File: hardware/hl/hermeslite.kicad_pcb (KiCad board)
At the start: 4 copper layers, 150 x 100 mm, 291 parts, among them CN1 USBBlaster2, CN2 PS, CN3 MagJack, CN4 IO8, CN5 IO8, J1 JNC, J10 JNC, J11 JNC, J12 JNO, J13 JNO, J14 JNC, J16 JNO, J17 JNO, J18 JNC, J2 JNC, J22 JNC, J3 JNO, J4 JNO, J7 JNO, J8 JNO, J9 JNC, Q1 DMP3099L, T2 8:1 Z, U1 EEPROM, U16 ST1S10, U17 TPS730, U2 FPGA, U3 ST1S10, U4 KSZ9031RN, U5 MCP4716, U6 5P49V5923, U7 AD9866BCPZ, X1 25MHz, X2 38.4MHz, X3 38.4MHz

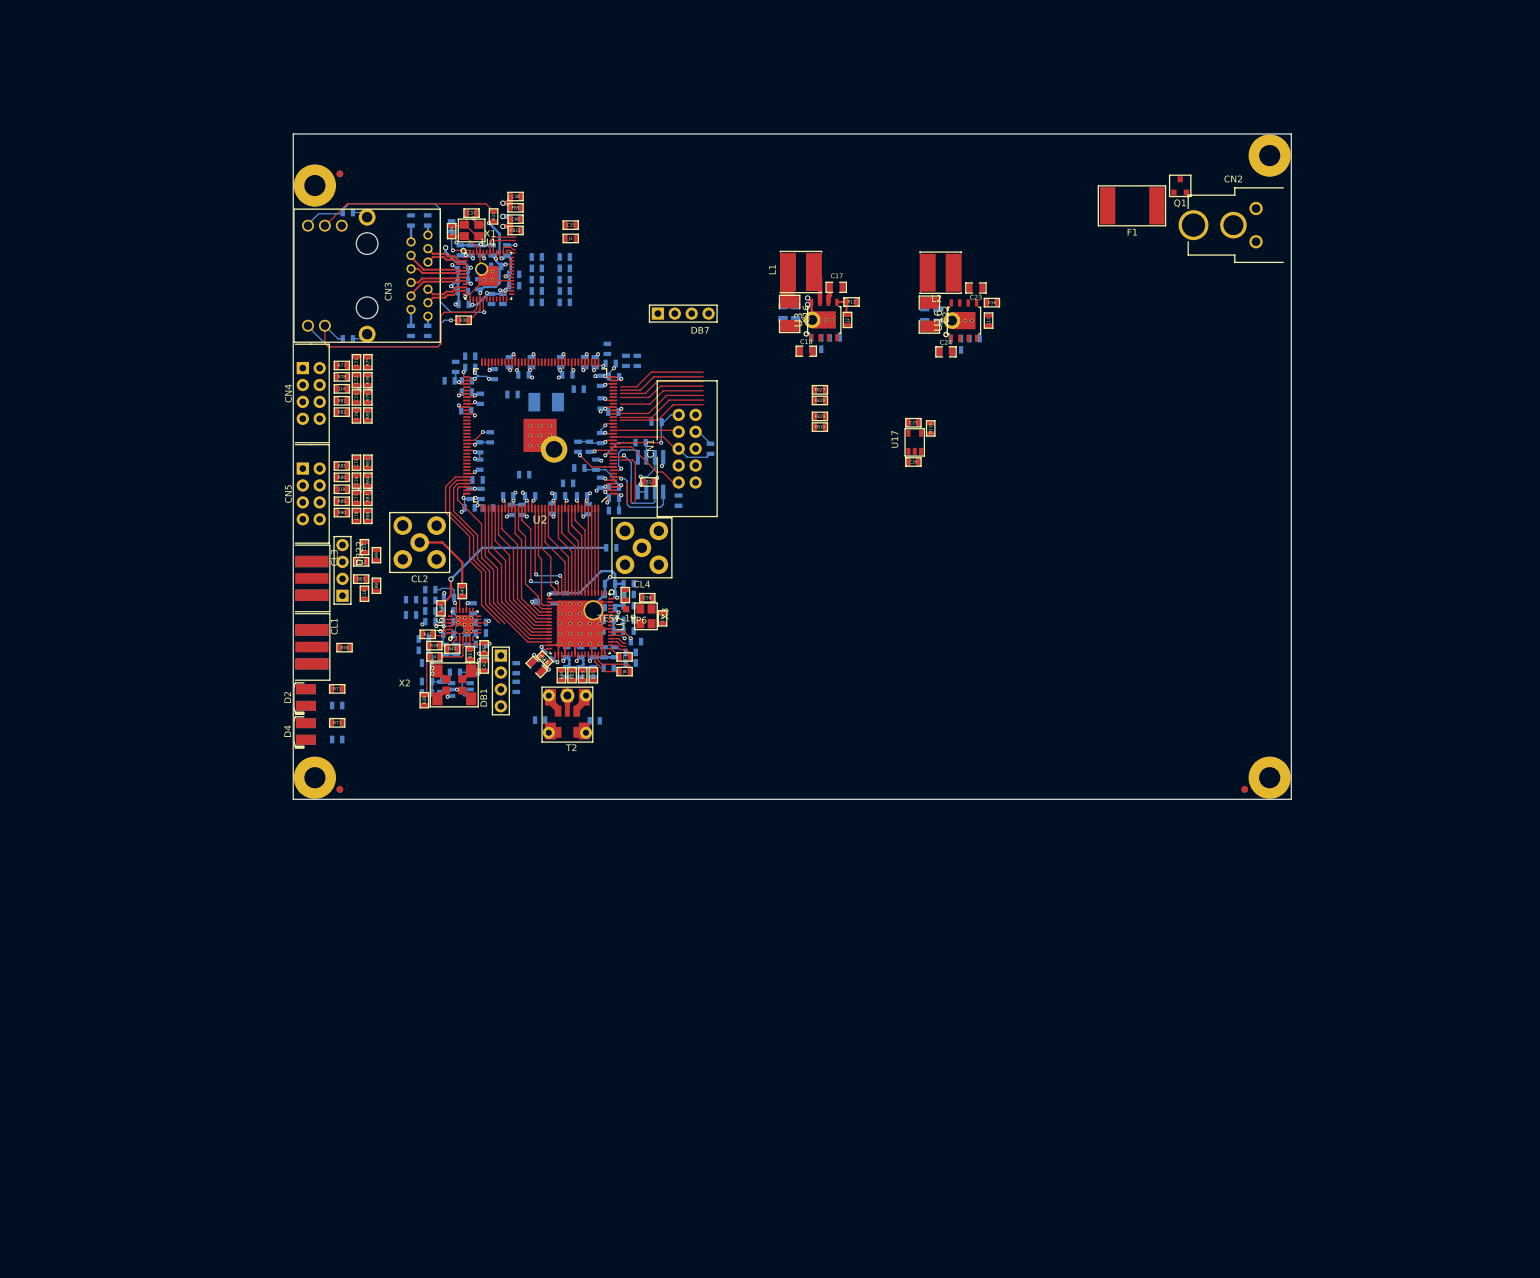
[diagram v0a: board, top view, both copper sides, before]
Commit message: Updates to layout
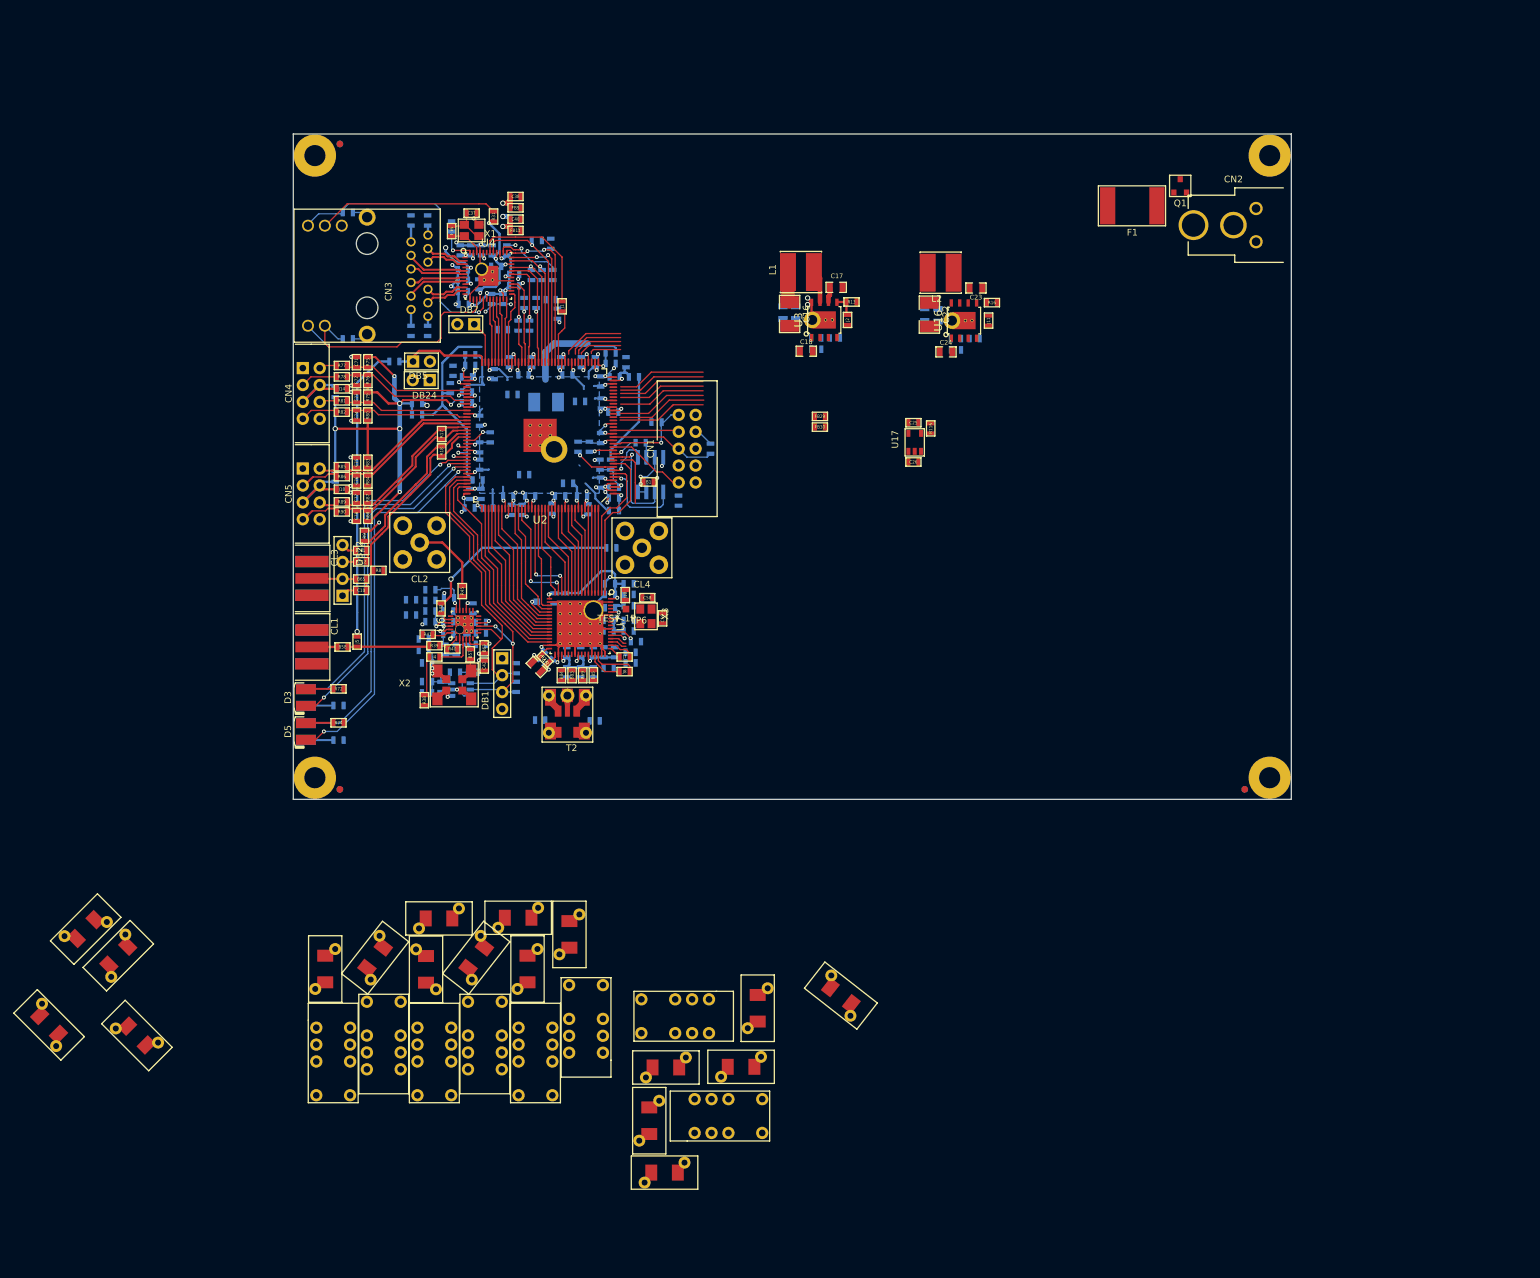
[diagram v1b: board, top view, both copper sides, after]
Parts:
- added DB24: RFD2b, HERMESLITE:2x1, F.Cu at (90.5, 77.0)
- added DB5: RFD2a, HERMESLITE:2x1, F.Cu at (88.0, 74.2)
- added J23: JNO, HERMESLITE:SMD-0603, B.Cu at (85.2, 74.2)
- added J5: JNO, HERMESLITE:SMD-0603, F.Cu at (79.6, 116.3)
- added R17: DNI, HERMESLITE:SMD-0603, F.Cu at (92.3, 85.1)
- added R18: DNI, HERMESLITE:SMD-0603, F.Cu at (92.3, 87.7)
- added REF**: inductor, HERMESLITE:inductor, F.Cu at (139.8, 171.4)
- added REF**: inductor, HERMESLITE:inductor, F.Cu at (105.2, 165.5)
- added REF**: DPDT, HERMESLITE:DPDT, F.Cu at (106.4, 179.4)
- added REF**: inductor, HERMESLITE:inductorrev, F.Cu at (90.0, 165.6)
- added REF**: DPDT, HERMESLITE:DPDT, F.Cu at (98.8, 175.5)
- added REF**: DPDT, HERMESLITE:DPDT, F.Cu at (91.2, 179.4)
- added REF**: inductor, HERMESLITE:inductorrev, F.Cu at (97.5, 163.8)
- added REF**: inductor, HERMESLITE:inductor, F.Cu at (152.3, 169.5)
- added REF**: inductor, HERMESLITE:inductorrev, F.Cu at (91.9, 157.9)
- added REF**: inductor, HERMESLITE:inductorrev, F.Cu at (126.0, 180.3)
- added REF**: inductor, HERMESLITE:inductor, F.Cu at (74.8, 165.5)
- added REF**: inductor, HERMESLITE:inductorrev, F.Cu at (137.3, 180.2)
- added REF**: inductor, HERMESLITE:inductor, F.Cu at (33.3, 173.9)
- added REF**: inductor, HERMESLITE:inductorrev, F.Cu at (46.5, 175.5)
- added REF**: inductor, HERMESLITE:inductorrev, F.Cu at (43.7, 163.5)
- added REF**: DPDT, HERMESLITE:DPDT, F.Cu at (83.6, 175.5)
- added REF**: inductor, HERMESLITE:inductor, F.Cu at (38.8, 159.5)
- added REF**: DPDT, HERMESLITE:DPDT, F.Cu at (76.0, 179.4)
- added REF**: inductor, HERMESLITE:inductorrev, F.Cu at (82.3, 163.8)
- added REF**: DPDT, HERMESLITE:DPDT, F.Cu at (127.4, 172.6)
- added REF**: inductor, HERMESLITE:inductorrev, F.Cu at (125.8, 196.1)
- added REF**: inductor, HERMESLITE:inductor, F.Cu at (123.5, 188.3)
- added REF**: inductor, HERMESLITE:inductor, F.Cu at (111.5, 160.3)
- added REF**: inductor, HERMESLITE:inductorrev, F.Cu at (103.8, 157.8)
- added REF**: DPDT, HERMESLITE:DPDT, F.Cu at (135.4, 187.6)
- added REF**: DPDT, HERMESLITE:DPDT, F.Cu at (114.0, 173.0)
- C35, D2, D4, FB27, FB28, R30, R71, R73: moved to B.Cu
- D3, D5, R72, R74: moved to F.Cu
- DB22: value RFD4d -> RFD4f
- DB7: value RFD4d -> RFD2b; footprint HERMESLITE:4x1 -> HERMESLITE:2x1
- moved FB28 60.6 mm to (88.6, 82.2), turned to 180 degrees
- moved FB27 60.6 mm to (88.6, 80.5), turned to 180 degrees
- moved DB7 27.6 mm to (97.2, 68.6), turned to 180 degrees
- moved C35 13.4 mm to (109.7, 67.0), turned to 270 degrees
- moved J1 10.3 mm to (110.4, 65.9), turned to 270 degrees
- moved R72 7.60 mm to (76.8, 123.4)
- moved R29 6.74 mm to (108.7, 64.9), turned to 180 degrees
- moved R22 6.10 mm to (104.7, 65.4), turned to 270 degrees
- moved R30 6.06 mm to (101.5, 69.4)
- moved R23 5.32 mm to (105.5, 68.8), turned to 90 degrees
- moved D3 5.10 mm to (70.9, 124.7), turned to 270 degrees
- moved D5 5.10 mm to (70.9, 129.8), turned to 270 degrees
- moved J17 4.79 mm to (76.3, 91.5), turned to 270 degrees
- moved FB6 4.73 mm to (117.7, 89.7), turned to 270 degrees
- moved R24 4.66 mm to (106.5, 65.4), turned to 270 degrees
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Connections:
- DB7 pad 1: Veth -> Net-(DB7-Pad1)
- DB7 pad 2: Net-(DB7-Pad2) -> GND
- R74 pad 1: Vlvds -> +3V3
- U2 pad 101: (no net) -> Net-(D5-Pad1)
- U2 pad 71: Net-(DB7-Pad2) -> Net-(DB7-Pad1)
- U2 pad 72: Net-(DB7-Pad3) -> Net-(DB5-Pad1)
- U2 pad 76: Net-(C71-Pad1) -> Net-(DB24-Pad1)
- U2 pad 77: Net-(C72-Pad1) -> Net-(C71-Pad1)
- U2 pad 80: Net-(C73-Pad1) -> Net-(C72-Pad1)
- U2 pad 83: Net-(C74-Pad1) -> Net-(C73-Pad1)
- U2 pad 85: Net-(D5-Pad1) -> Net-(C74-Pad1)
- U2 pad 90: Net-(B65-Pad2) -> Net-(B112-Pad2)
- U2 pad 91: Net-(B112-Pad2) -> Net-(B65-Pad2)
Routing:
- net Vlvds: track 2.21 -> 78.3 mm, vias 1 -> 7
- net Net-(D5-Pad1): track 0.00 -> 56.6 mm, vias 0 -> 2
- net Net-(D4-Pad1): track 0.00 -> 55.8 mm, vias 0 -> 1
- net Net-(D3-Pad1): track 0.00 -> 52.0 mm, vias 0 -> 2
- net Net-(D2-Pad1): track 0.00 -> 51.2 mm, vias 0 -> 1
- net +2V5: track 0.00 -> 48.3 mm, vias 0 -> 1
- net Net-(J23-Pad1): track 0.00 -> 44.3 mm, vias 0 -> 1
- net (no net): track 121.4 -> 162.9 mm
- net +1V2: track 53.3 -> 92.6 mm
- net Net-(B65-Pad2): track 0.00 -> 31.6 mm
- net Net-(B112-Pad2): track 0.00 -> 30.1 mm
- net GND: track 193.7 -> 218.9 mm, vias 56 -> 72
- net Net-(C78-Pad1): track 0.00 -> 24.9 mm
- net SCL: track 27.0 -> 51.7 mm, vias 0 -> 2
- net Net-(C77-Pad1): track 0.00 -> 24.6 mm
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- added copper zone on B.Cu, net +1V2
- added copper zone on In1.Cu, net GND
- added copper zone on In2.Cu, net Veth

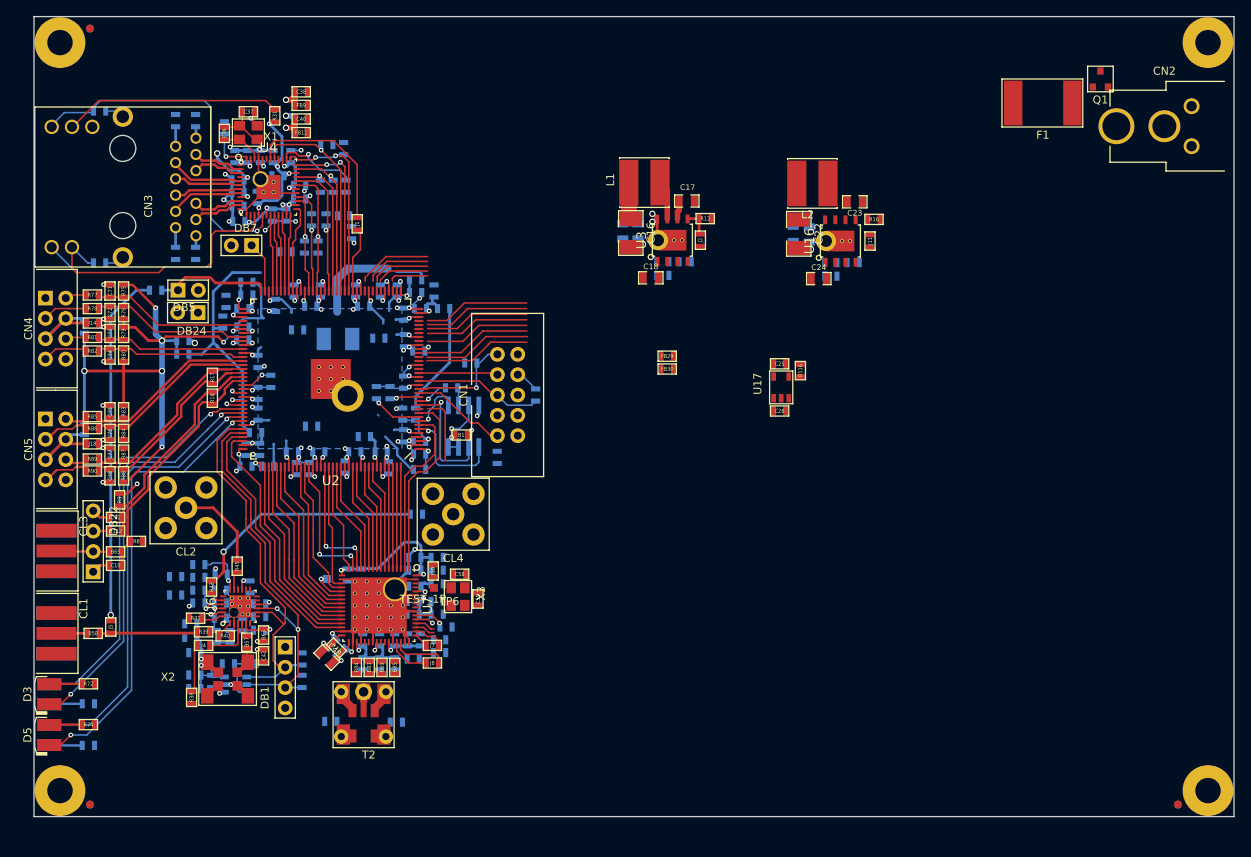
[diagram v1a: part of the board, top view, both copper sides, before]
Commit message: Layout and routing work
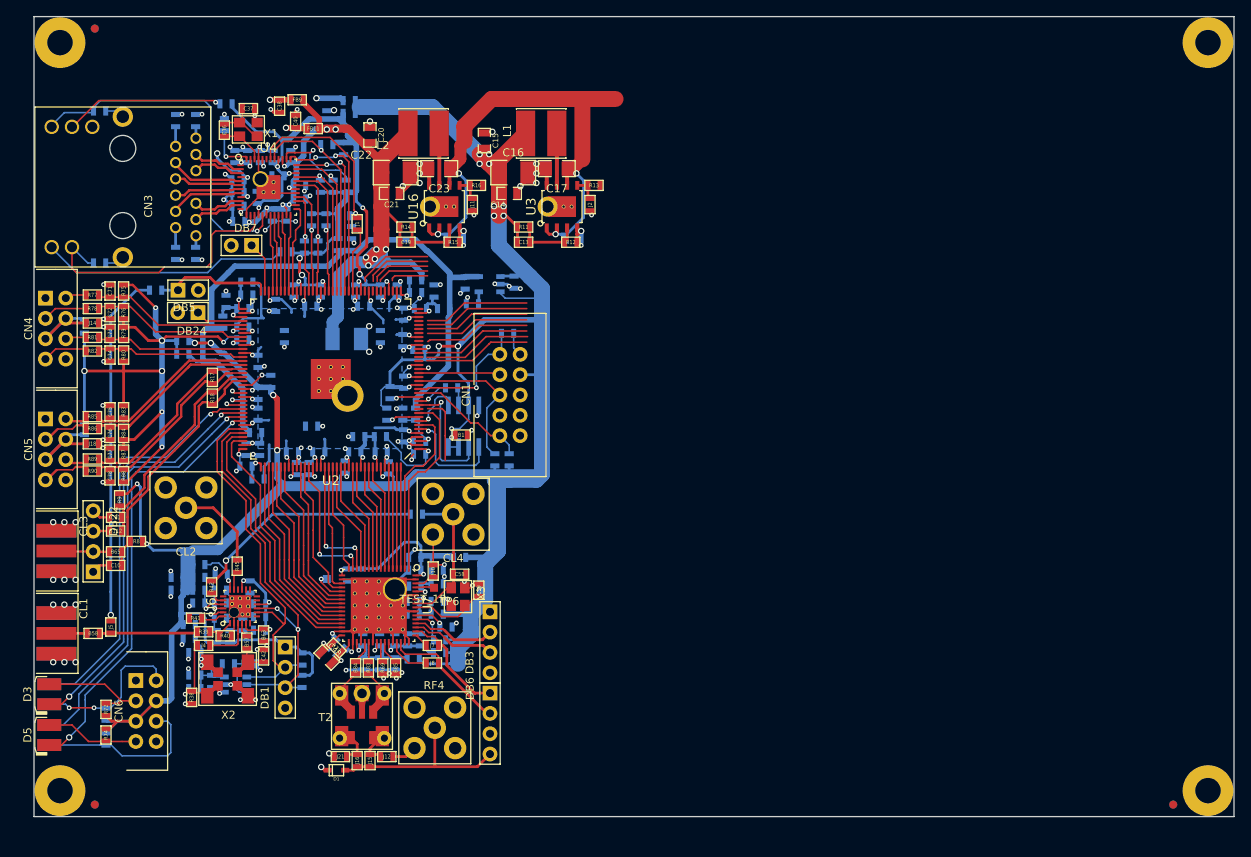
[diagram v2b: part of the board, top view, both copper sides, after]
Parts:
- removed CN2: PS, HERMESLITE:POWER
- removed F1: 3A@20V, HERMESLITE:FUSE
- removed Q1: DMP3099L, HERMESLITE:SOT23_3
- added CN6: IO8, HERMESLITE:IO, F.Cu at (84.0, 126.8)
- added D1: TVS, HERMESLITE:SOD323, F.Cu at (107.8, 134.2)
- added DB3: RFD4b, HERMESLITE:4x1, F.Cu at (127.0, 114.4)
- added DB6: RFD4b, HERMESLITE:4x1, F.Cu at (127.0, 124.6)
- added J15: JNC, HERMESLITE:SMD-0603, F.Cu at (112.0, 133.0)
- added J21: JNC, HERMESLITE:SMD-0603, F.Cu at (108.3, 132.5)
- added RF4: BNC, HERMESLITE:SMAVERT, F.Cu at (120.1, 128.9)
- B116, C18, C24, C25, C26, FB29, FB30, R31, U17: moved to B.Cu
- C13, C14, C15, C19, C20, C21, J12, J16, R11, R12, R14, R15: moved to F.Cu
- C17, C23: footprint HERMESLITE:SMD-0805 -> HERMESLITE:SMD-1206
- moved C20 56.3 mm to (112.0, 54.8), turned to 90 degrees
- moved R14 53.3 mm to (116.5, 66.3)
- moved C19 53.3 mm to (116.5, 68.2)
- moved C23 52.1 mm to (120.7, 59.0), turned to 180 degrees
- moved C22 51.0 mm to (115.2, 59.5), turned to 0 degrees
- moved C21 50.5 mm to (114.7, 62.1), turned to 0 degrees
- moved R15 50.1 mm to (122.4, 68.2)
- moved FB29 50.0 mm to (109.4, 52.1), turned to 180 degrees
- moved J11 49.9 mm to (124.8, 63.5)
- moved R16 49.9 mm to (125.3, 61.1)
- moved U16 49.7 mm to (121.3, 63.8)
- moved L2 49.0 mm to (118.7, 54.6)
- moved C24 45.8 mm to (122.6, 67.7), turned to 0 degrees
- moved FB30 44.0 mm to (108.0, 68.5), turned to 90 degrees
- moved B116 41.8 mm to (124.8, 75.9), turned to 180 degrees
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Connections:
- D2 pad 2: Net-(D2-Pad2) -> Net-(CN6-Pad2)
- D3 pad 2: Net-(D3-Pad2) -> Net-(CN6-Pad3)
- D4 pad 2: Net-(D4-Pad2) -> Net-(CN6-Pad6)
- D5 pad 2: Net-(D5-Pad2) -> Net-(CN6-Pad7)
- R71 pad 1: +3V3 -> Net-(CN6-Pad2)
- R71 pad 2: Net-(D2-Pad2) -> +3V3
- R72 pad 1: +3V3 -> Net-(CN6-Pad3)
- R72 pad 2: Net-(D3-Pad2) -> +3V3
- R73 pad 1: +3V3 -> Net-(CN6-Pad6)
- R73 pad 2: Net-(D4-Pad2) -> +3V3
- R74 pad 1: +3V3 -> Net-(CN6-Pad7)
- R74 pad 2: Net-(D5-Pad2) -> +3V3
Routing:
- net +3V3: track 42.0 -> 410.4 mm, vias 11 -> 25
- net GND: track 218.9 -> 368.1 mm, vias 72 -> 144
- net +1V2: track 92.6 -> 183.5 mm, vias 20 -> 27
- net Veth: track 29.0 -> 101.3 mm, vias 8 -> 11
- net Net-(C17-Pad1): track 2.34 -> 69.9 mm, vias 0 -> 4
- net +2V5: track 48.3 -> 85.5 mm
- net Net-(CN3-Pad14): track 4.46 -> 31.0 mm
- net Net-(C53-Pad2): track 0.00 -> 23.8 mm
- net Net-(CN6-Pad6): track 0.00 -> 22.3 mm
- net Net-(CN6-Pad2): track 0.00 -> 19.4 mm, vias 0 -> 2
- net Net-(C58-Pad1): track 0.00 -> 18.8 mm
- net Net-(CN6-Pad3): track 0.00 -> 13.7 mm
- net Net-(CN6-Pad7): track 0.00 -> 12.4 mm
- net (no net): track 162.9 -> 151.7 mm
- net Net-(DB6-Pad1): track 3.93 -> 14.1 mm
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- removed copper zone on In2.Cu, net Veth
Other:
- board text added: "10V Power Supply"
- board text added: "Add power supply taps 3.3, 2.5, 1.2"
- board text added: "Slow ADC? Digital Bias? Bus Expander?"
- board text removed: "Power Supply"
